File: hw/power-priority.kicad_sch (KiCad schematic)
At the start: 18 parts, among them IC7702 LM74800QDRRRQ1, IC7703 LM74800QDRRRQ1, Q7706 IPB026N06NATMA1, Q7707 IPB026N06NATMA1, Q7714 IPB026N06NATMA1, Q7715 IPB026N06NATMA1

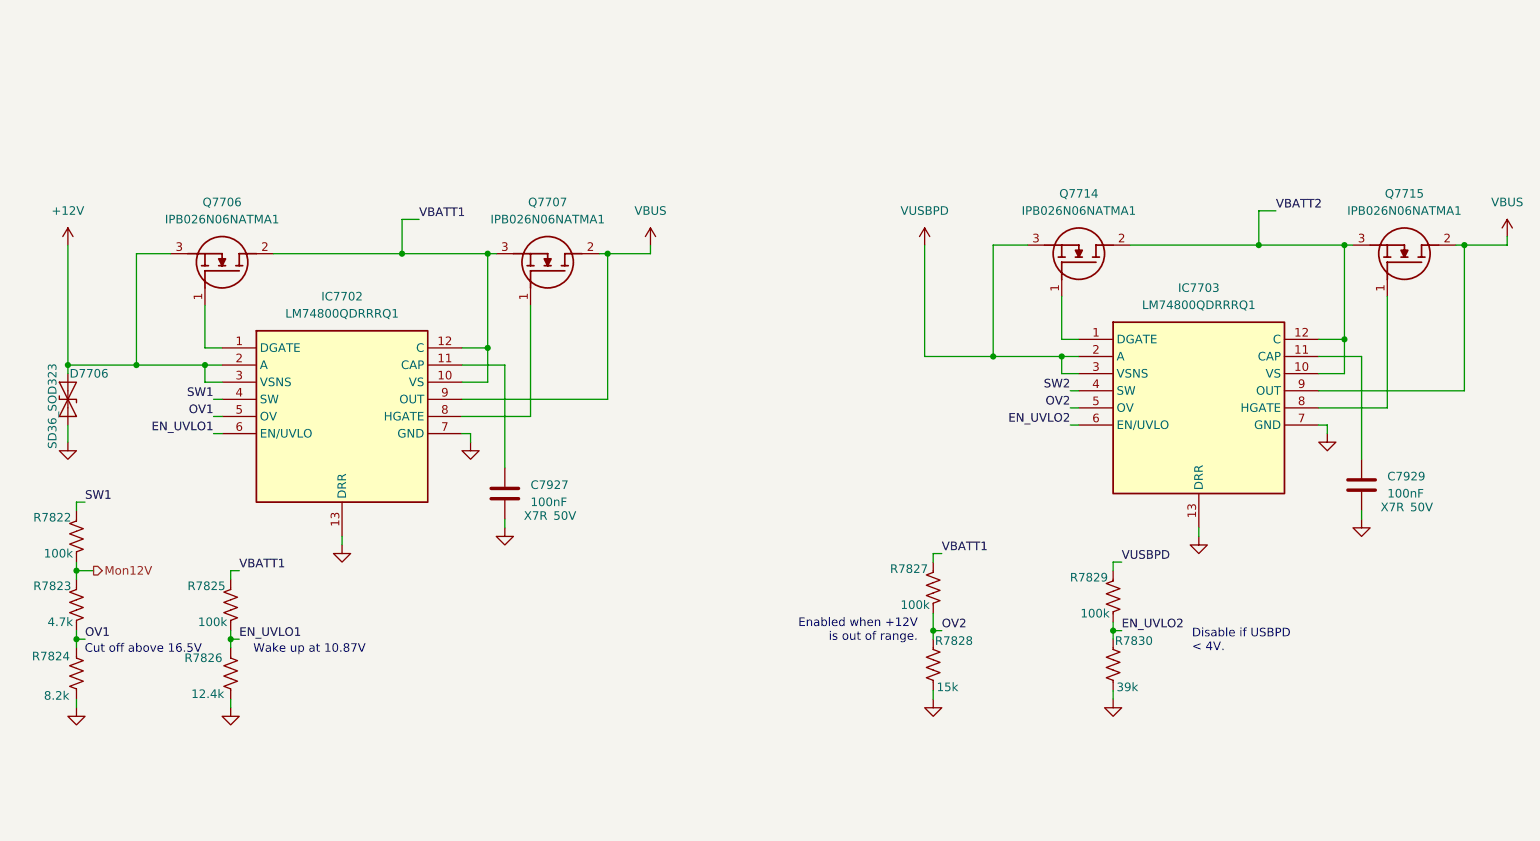
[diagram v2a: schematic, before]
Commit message: Fixed GPIO assignments. Fixed symbol for GRL2-2 relays.
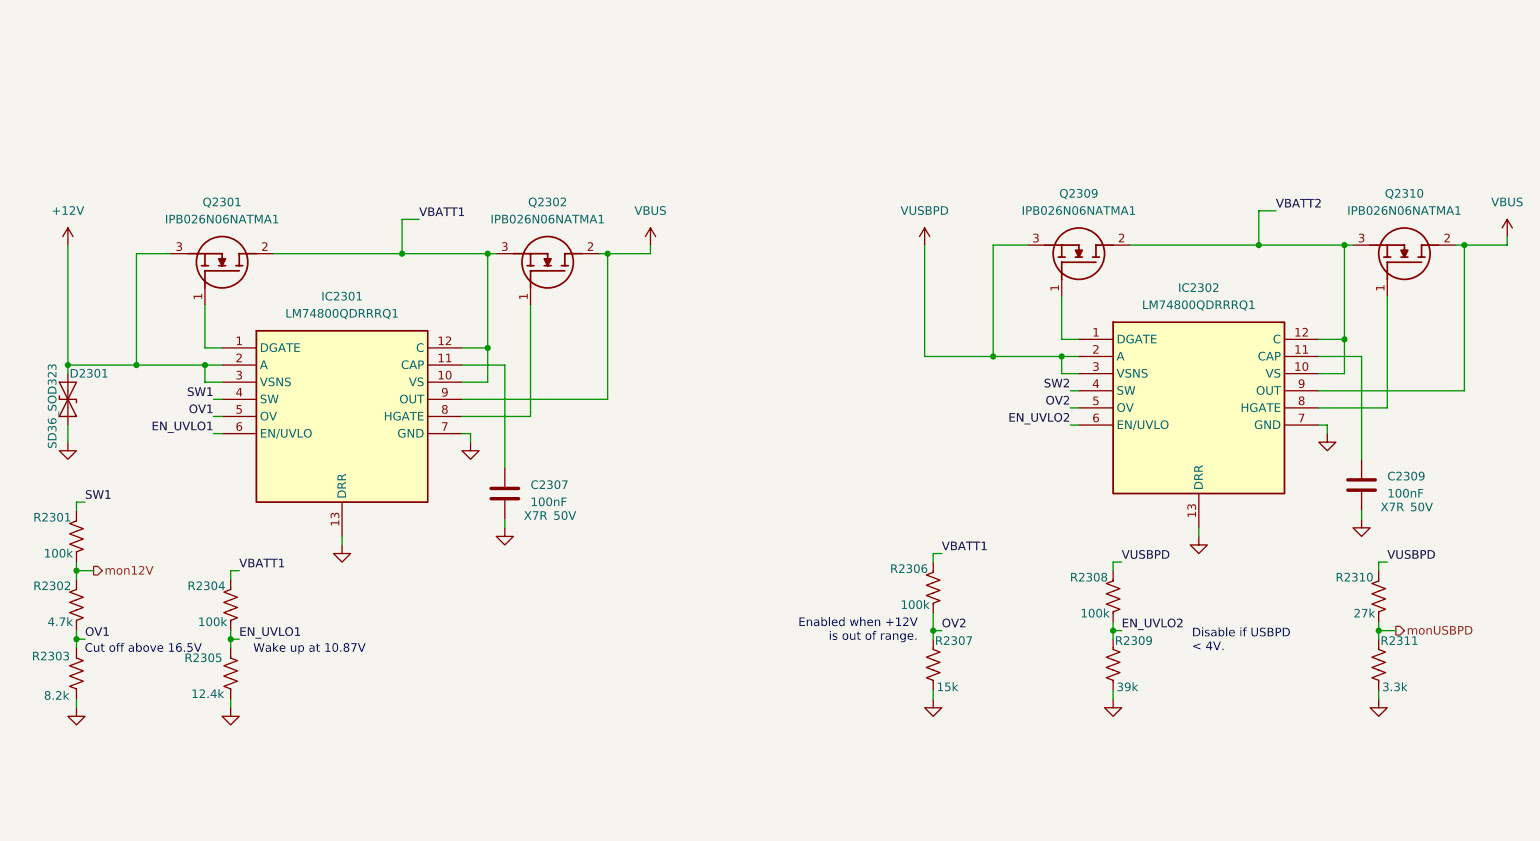
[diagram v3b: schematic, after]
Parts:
- added R2310: 27k, symbol Device:R_US
- added R2311: 3.3k, symbol Device:R_US
- C2307: renamed from C7927; footprint (none) -> Capacitor_SMD:C_0805_2012Metric
- C2309: renamed from C7929; footprint (none) -> Capacitor_SMD:C_0805_2012Metric
- renumbered D7706 to D2301, IC7702 to IC2301, IC7703 to IC2302, Q7706 to Q2301, Q7707 to Q2302, Q7714 to Q2309, Q7715 to Q2310, R7822 to R2301, R7823 to R2302, R7824 to R2303, R7825 to R2304, R7826 to R2305, R7827 to R2306, R7828 to R2307, R7829 to R2308, R7830 to R2309
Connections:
- net GND: now also R2311.2
- net VUSBPD: now also R2310.1
- net Mon12V renamed mon12V
- new net monUSBPD: R2310.2, R2311.1

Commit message: I think I have finished the relay conversion and 5V SPI I/O expander crap
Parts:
- renumbered C2307 to C7958, C2309 to C7960, D2301 to D7736, IC2301 to IC7703, IC2302 to IC7704, Q2301 to Q7706, Q2302 to Q7707, Q2309 to Q7714, Q2310 to Q7715, R2301 to R7844, R2302 to R7845, R2303 to R7846, R2304 to R7847, R2305 to R7848, R2306 to R7849, R2307 to R7850, R2308 to R7851, R2309 to R7852, R2310 to R7853, R2311 to R7854

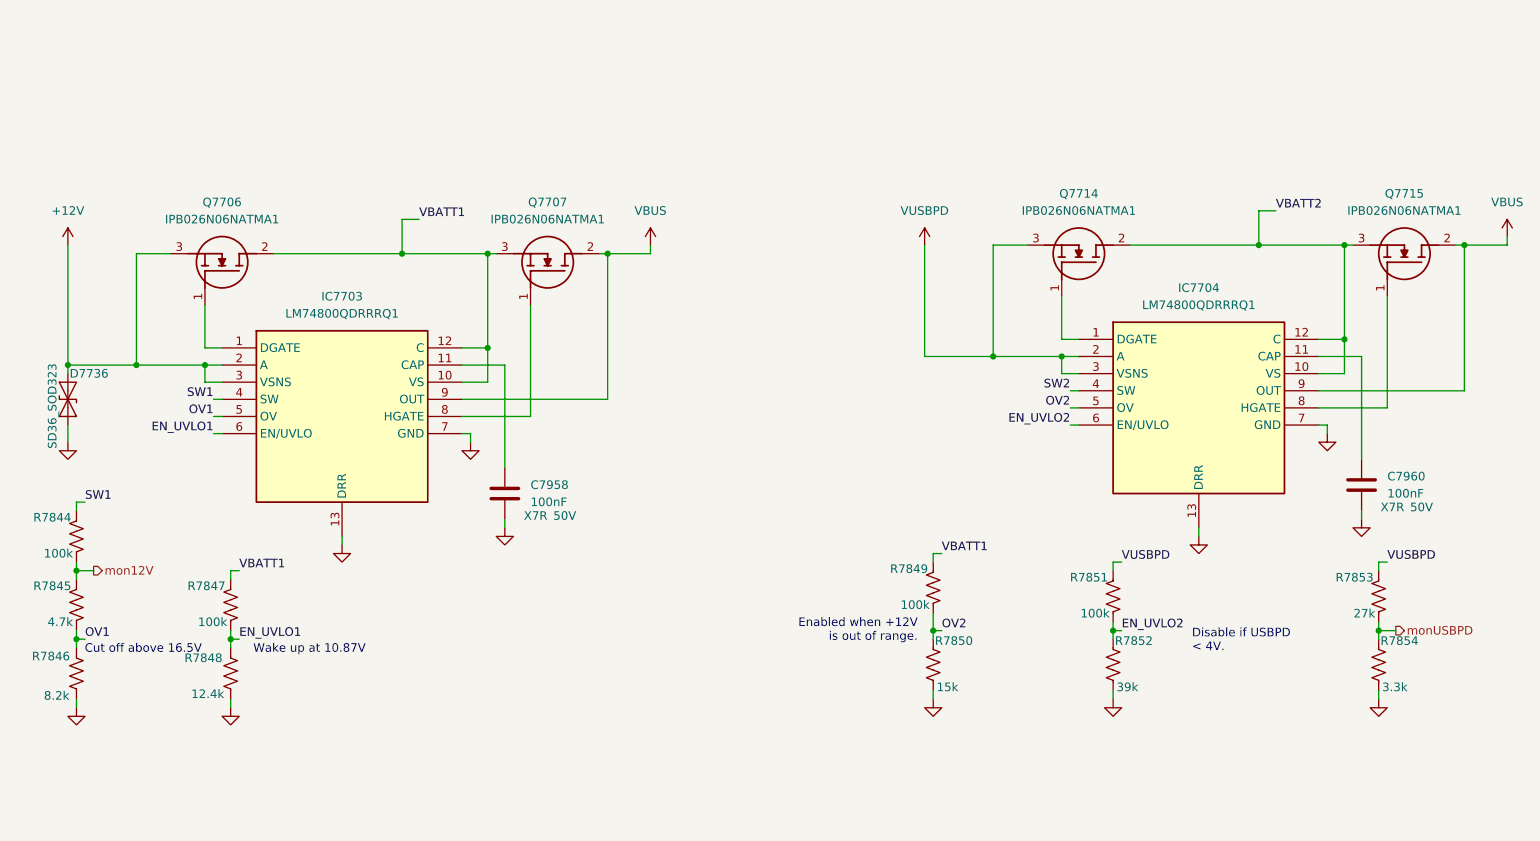
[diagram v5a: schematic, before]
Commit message: Starting to build guanella transformers. Mostly converted to 1-2-1 tx, but FPGA still to do.
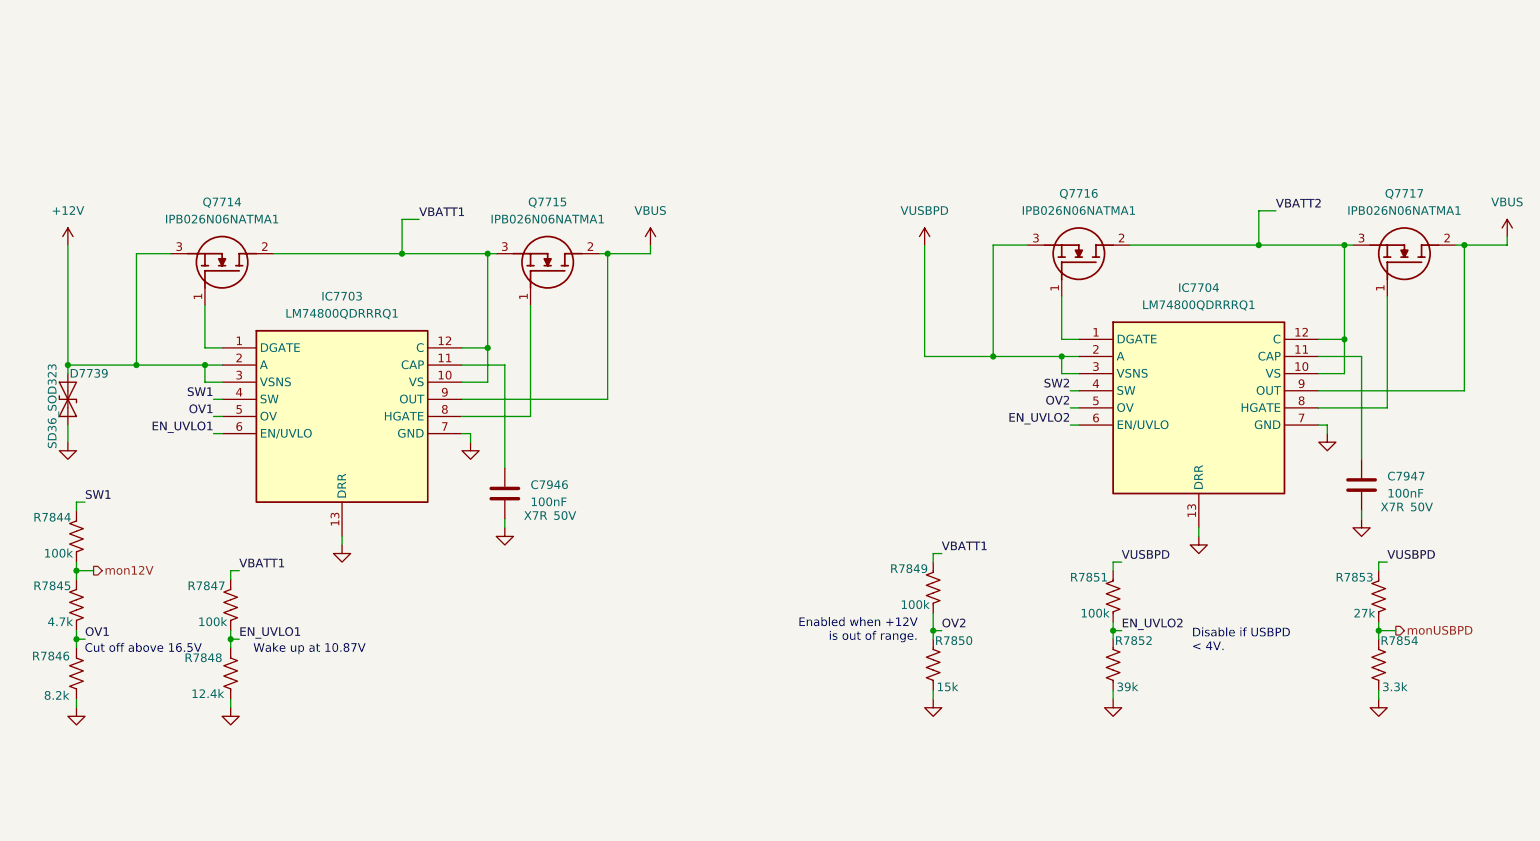
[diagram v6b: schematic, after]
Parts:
- renumbered C7958 to C7946, C7960 to C7947, D7736 to D7739, Q7706 to Q7714, Q7707 to Q7715, Q7714 to Q7716, Q7715 to Q7717
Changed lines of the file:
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@@
 		(dnp no)
 		(fields_autoplaced yes)
-		(property "Reference" "#PWR08094"
+		(property "Reference" "#PWR08104"
 			(at 127 72.39 0)
 			(effects
@@
 			(project "NexRig"
 				(path "/8ae46c04-d01a-4756-8774-512b694bfaff/cbf7569b-90aa-4e1a-84a7-d4153f6242b6/b06410ec-4c8e-4291-9691-3a63bcaba95c"
-					(reference "#PWR08094")
+					(reference "#PWR08104")
 					(unit 1)
 				)
@@
 		(dnp no)
 		(fields_autoplaced yes)
-		(property "Reference" "#PWR08090"
+		(property "Reference" "#PWR08102"
 			(at 100.33 104.14 0)
 			(effects
@@
 			(project "NexRig"
 				(path "/8ae46c04-d01a-4756-8774-512b694bfaff/cbf7569b-90aa-4e1a-84a7-d4153f6242b6/b06410ec-4c8e-4291-9691-3a63bcaba95c"
-					(reference "#PWR08090")
+					(reference "#PWR08102")
 					(unit 1)
 				)
@@
 		(dnp no)
 		(fields_autoplaced yes)
-		(property "Reference" "#PWR08081"
+		(property "Reference" "#PWR08097"
 			(at 40.64 72.39 0)
 			(effects
@@
 			(project "NexRig"
 				(path "/8ae46c04-d01a-4756-8774-512b694bfaff/cbf7569b-90aa-4e1a-84a7-d4153f6242b6/b06410ec-4c8e-4291-9691-3a63bcaba95c"
-					(reference "#PWR08081")
+					(reference "#PWR08097")
 					(unit 1)
 				)
@@
 		(dnp no)
 		(fields_autoplaced yes)
-		(property "Reference" "#PWR08099"
+		(property "Reference" "#PWR08105"
 			(at 167.64 72.39 0)
 			(effects
@@
 			(project "NexRig"
 				(path "/8ae46c04-d01a-4756-8774-512b694bfaff/cbf7569b-90aa-4e1a-84a7-d4153f6242b6/b06410ec-4c8e-4291-9691-3a63bcaba95c"
-					(reference "#PWR08099")
+					(reference "#PWR08105")
 					(unit 1)
 				)
@@
 		(dnp no)
 		(fields_autoplaced yes)
-		(property "Reference" "#PWR08108"
+		(property "Reference" "#PWR08111"
 			(at 234.95 142.24 0)
 			(effects
@@
 			(project "NexRig"
 				(path "/8ae46c04-d01a-4756-8774-512b694bfaff/cbf7569b-90aa-4e1a-84a7-d4153f6242b6/b06410ec-4c8e-4291-9691-3a63bcaba95c"
-					(reference "#PWR08108")
+					(reference "#PWR08111")
 					(unit 1)
 				)
@@
 		(dnp no)
 		(fields_autoplaced yes)
-		(property "Reference" "#PWR08087"
+		(property "Reference" "#PWR08101"
 			(at 81.28 119.38 0)
 			(effects
@@
 			(project "NexRig"
 				(path "/8ae46c04-d01a-4756-8774-512b694bfaff/cbf7569b-90aa-4e1a-84a7-d4153f6242b6/b06410ec-4c8e-4291-9691-3a63bcaba95c"
-					(reference "#PWR08087")
+					(reference "#PWR08101")
 					(unit 1)
 				)
@@
 		(dnp no)
 		(fields_autoplaced yes)
-		(property "Reference" "#PWR08106"
+		(property "Reference" "#PWR08109"
 			(at 227.33 102.87 0)
 			(effects
@@
 			(project "NexRig"
 				(path "/8ae46c04-d01a-4756-8774-512b694bfaff/cbf7569b-90aa-4e1a-84a7-d4153f6242b6/b06410ec-4c8e-4291-9691-3a63bcaba95c"
-					(reference "#PWR08106")
+					(reference "#PWR08109")
 					(unit 1)
 				)
@@
 		(on_board yes)
 		(dnp no)
-		(property "Reference" "D7736"
+		(property "Reference" "D7739"
 			(at 40.894 87.63 90)
 			(effects
@@
 			(project ""
 				(path "/8ae46c04-d01a-4756-8774-512b694bfaff/cbf7569b-90aa-4e1a-84a7-d4153f6242b6/b06410ec-4c8e-4291-9691-3a63bcaba95c"
-					(reference "D7736")
+					(reference "D7739")
 					(unit 1)
 				)
@@
 		(dnp no)
 		(fields_autoplaced yes)
-		(property "Reference" "#PWR08103"
+		(property "Reference" "#PWR08108"
 			(at 208.28 118.11 0)
 			(effects
@@
 			(project "NexRig"
 				(path "/8ae46c04-d01a-4756-8774-512b694bfaff/cbf7569b-90aa-4e1a-84a7-d4153f6242b6/b06410ec-4c8e-4291-9691-3a63bcaba95c"
-					(reference "#PWR08103")
+					(reference "#PWR08108")
 					(unit 1)
 				)
@@
 		(dnp no)
 		(fields_autoplaced yes)
-		(property "Reference" "#PWR08082"
+		(property "Reference" "#PWR08098"
 			(at 40.64 104.14 0)
 			(effects
@@
 			(project "NexRig"
 				(path "/8ae46c04-d01a-4756-8774-512b694bfaff/cbf7569b-90aa-4e1a-84a7-d4153f6242b6/b06410ec-4c8e-4291-9691-3a63bcaba95c"
-					(reference "#PWR08082")
+					(reference "#PWR08098")
 					(unit 1)
 				)
@@
 		(on_board yes)
 		(dnp no)
-		(property "Reference" "Q7714"
+		(property "Reference" "Q7716"
 			(at 190.5 60.96 90)
 			(effects
@@
 			(project "NexRig"
 				(path "/8ae46c04-d01a-4756-8774-512b694bfaff/cbf7569b-90aa-4e1a-84a7-d4153f6242b6/b06410ec-4c8e-4291-9691-3a63bcaba95c"
-					(reference "Q7714")
+					(reference "Q7716")
 					(unit 1)
 				)
@@
 		(on_board yes)
 		(dnp no)
-		(property "Reference" "Q7707"
+		(property "Reference" "Q7715"
 			(at 111.76 62.23 90)
 			(effects
@@
 			(project "NexRig"
 				(path "/8ae46c04-d01a-4756-8774-512b694bfaff/cbf7569b-90aa-4e1a-84a7-d4153f6242b6/b06410ec-4c8e-4291-9691-3a63bcaba95c"
-					(reference "Q7707")
+					(reference "Q7715")
 					(unit 1)
 				)
@@
 		(dnp no)
 		(fields_autoplaced yes)
-		(property "Reference" "#PWR08084"
+		(property "Reference" "#PWR08099"
 			(at 41.91 143.51 0)
 			(effects
@@
 			(project "NexRig"
 				(path "/8ae46c04-d01a-4756-8774-512b694bfaff/cbf7569b-90aa-4e1a-84a7-d4153f6242b6/b06410ec-4c8e-4291-9691-3a63bcaba95c"
-					(reference "#PWR08084")
+					(reference "#PWR08099")
 					(unit 1)
 				)
@@
 		(dnp no)
 		(fields_autoplaced yes)
-		(property "Reference" "#PWR08107"
+		(property "Reference" "#PWR08110"
 			(at 232.41 115.57 0)
 			(effects
@@
 			(project "NexRig"
 				(path "/8ae46c04-d01a-4756-8774-512b694bfaff/cbf7569b-90aa-4e1a-84a7-d4153f6242b6/b06410ec-4c8e-4291-9691-3a63bcaba95c"
-					(reference "#PWR08107")
+					(reference "#PWR08110")
 					(unit 1)
 				)
@@
 		(on_board yes)
 		(dnp no)
-		(property "Reference" "C7960"
+		(property "Reference" "C7947"
 			(at 236.22 102.8699 0)
 			(effects
@@
 			(project "NexRig"
 				(path "/8ae46c04-d01a-4756-8774-512b694bfaff/cbf7569b-90aa-4e1a-84a7-d4153f6242b6/b06410ec-4c8e-4291-9691-3a63bcaba95c"
-					(reference "C7960")
+					(reference "C7947")
 					(unit 1)
 				)
@@
 		(dnp no)
 		(fields_autoplaced yes)
-		(property "Reference" "#PWR08086"
+		(property "Reference" "#PWR08100"
 			(at 64.77 143.51 0)
 			(effects
@@
 			(project "NexRig"
 				(path "/8ae46c04-d01a-4756-8774-512b694bfaff/cbf7569b-90aa-4e1a-84a7-d4153f6242b6/b06410ec-4c8e-4291-9691-3a63bcaba95c"
-					(reference "#PWR08086")
+					(reference "#PWR08100")
 					(unit 1)
 				)
@@
 		(dnp no)
 		(fields_autoplaced yes)
-		(property "Reference" "#PWR08111"
+		(property "Reference" "#PWR08112"
 			(at 254 71.12 0)
 			(effects
@@
 			(project "NexRig"
 				(path "/8ae46c04-d01a-4756-8774-512b694bfaff/cbf7569b-90aa-4e1a-84a7-d4153f6242b6/b06410ec-4c8e-4291-9691-3a63bcaba95c"
-					(reference "#PWR08111")
+					(reference "#PWR08112")
 					(unit 1)
 				)
@@
 		(dnp no)
 		(fields_autoplaced yes)
-		(property "Reference" "#PWR08091"
+		(property "Reference" "#PWR08103"
 			(at 105.41 116.84 0)
 			(effects
@@
 			(project "NexRig"
 				(path "/8ae46c04-d01a-4756-8774-512b694bfaff/cbf7569b-90aa-4e1a-84a7-d4153f6242b6/b06410ec-4c8e-4291-9691-3a63bcaba95c"
-					(reference "#PWR08091")
+					(reference "#PWR08103")
 					(unit 1)
 				)
@@
 		(dnp no)
 		(fields_autoplaced yes)
-		(property "Reference" "#PWR08102"
+		(property "Reference" "#PWR08107"
 			(at 195.58 142.24 0)
 			(effects
@@
 			(project "NexRig"
 				(path "/8ae46c04-d01a-4756-8774-512b694bfaff/cbf7569b-90aa-4e1a-84a7-d4153f6242b6/b06410ec-4c8e-4291-9691-3a63bcaba95c"
-					(reference "#PWR08102")
+					(reference "#PWR08107")
 					(unit 1)
 				)
@@
 		(dnp no)
 		(fields_autoplaced yes)
-		(property "Reference" "#PWR08100"
+		(property "Reference" "#PWR08106"
 			(at 168.91 142.24 0)
 			(effects
@@
 			(project "NexRig"
 				(path "/8ae46c04-d01a-4756-8774-512b694bfaff/cbf7569b-90aa-4e1a-84a7-d4153f6242b6/b06410ec-4c8e-4291-9691-3a63bcaba95c"
-					(reference "#PWR08100")
+					(reference "#PWR08106")
 					(unit 1)
 				)
@@
 		(on_board yes)
 		(dnp no)
-		(property "Reference" "C7958"
+		(property "Reference" "C7946"
 			(at 109.22 104.1399 0)
 			(effects
@@
 			(project "NexRig"
 				(path "/8ae46c04-d01a-4756-8774-512b694bfaff/cbf7569b-90aa-4e1a-84a7-d4153f6242b6/b06410ec-4c8e-4291-9691-3a63bcaba95c"
-					(reference "C7958")
+					(reference "C7946")
 					(unit 1)
 				)
@@
 		(on_board yes)
 		(dnp no)
-		(property "Reference" "Q7706"
+		(property "Reference" "Q7714"
 			(at 63.5 62.23 90)
 			(effects
@@
 			(project "NexRig"
 				(path "/8ae46c04-d01a-4756-8774-512b694bfaff/cbf7569b-90aa-4e1a-84a7-d4153f6242b6/b06410ec-4c8e-4291-9691-3a63bcaba95c"
-					(reference "Q7706")
+					(reference "Q7714")
 					(unit 1)
 				)
@@
 		(on_board yes)
 		(dnp no)
-		(property "Reference" "Q7715"
+		(property "Reference" "Q7717"
 			(at 238.76 60.96 90)
 			(effects
@@
 			(project "NexRig"
 				(path "/8ae46c04-d01a-4756-8774-512b694bfaff/cbf7569b-90aa-4e1a-84a7-d4153f6242b6/b06410ec-4c8e-4291-9691-3a63bcaba95c"
-					(reference "Q7715")
-					(unit 1)
-				)
+					(reference "Q7717")
+					(unit 1)
+				)

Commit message: Checkpoint. FPGA is mostly done (need a check!). Working on new LPFs. Need inductor footprints and to fix a bunch of broken/missing footprints.
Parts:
- C7946, C7947: footprint Capacitor_SMD:C_0805_2012Metric -> Capacitor_SMD:C_0603_1608Metric
- R7844, R7847, R7849, R7851: footprint (none) -> Resistor_SMD:R_0402_1005Metric
- R7845, R7846, R7848, R7850, R7852, R7853, R7854: footprint (none) -> Resistor_SMD:R_0603_1608Metric
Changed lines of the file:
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@@
 			)
 		)
-		(property "Footprint" ""
+		(property "Footprint" "Resistor_SMD:R_0603_1608Metric"
 			(at 196.596 131.064 90)
 			(effects
@@
 			)
 		)
-		(property "Footprint" ""
+		(property "Footprint" "Resistor_SMD:R_0603_1608Metric"
 			(at 42.926 132.334 90)
 			(effects
@@
 			)
 		)
-		(property "Footprint" ""
+		(property "Footprint" "Resistor_SMD:R_0402_1005Metric"
 			(at 63.754 122.174 90)
 			(effects
@@
 			)
 		)
-		(property "Footprint" ""
+		(property "Footprint" "Resistor_SMD:R_0402_1005Metric"
 			(at 40.894 112.014 90)
 			(effects
@@
 			)
 		)
-		(property "Footprint" ""
+		(property "Footprint" "Resistor_SMD:R_0402_1005Metric"
 			(at 167.894 119.634 90)
 			(effects
@@
 			)
 		)
-		(property "Footprint" ""
+		(property "Footprint" "Resistor_SMD:R_0603_1608Metric"
 			(at 235.966 131.064 90)
 			(effects
@@
 			)
 		)
-		(property "Footprint" ""
+		(property "Footprint" "Resistor_SMD:R_0603_1608Metric"
 			(at 65.786 132.334 90)
 			(effects
@@
 			)
 		)
-		(property "Footprint" ""
+		(property "Footprint" "Resistor_SMD:R_0402_1005Metric"
 			(at 194.564 120.904 90)
 			(effects
@@
 			)
 		)
-		(property "Footprint" "Capacitor_SMD:C_0805_2012Metric"
+		(property "Footprint" "Capacitor_SMD:C_0603_1608Metric"
 			(at 231.4448 107.95 0)
 			(effects
@@
 			)
 		)
-		(property "Footprint" ""
+		(property "Footprint" "Resistor_SMD:R_0603_1608Metric"
 			(at 233.934 120.904 90)
 			(effects
@@
 			)
 		)
-		(property "Footprint" ""
+		(property "Footprint" "Resistor_SMD:R_0603_1608Metric"
 			(at 169.926 131.064 90)
 			(effects
@@
 			)
 		)
-		(property "Footprint" "Capacitor_SMD:C_0805_2012Metric"
+		(property "Footprint" "Capacitor_SMD:C_0603_1608Metric"
 			(at 104.4448 109.22 0)
 			(effects
@@
 			)
 		)
-		(property "Footprint" ""
+		(property "Footprint" "Resistor_SMD:R_0603_1608Metric"
 			(at 40.894 122.174 90)
 			(effects
